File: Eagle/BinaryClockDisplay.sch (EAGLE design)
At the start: 44 parts

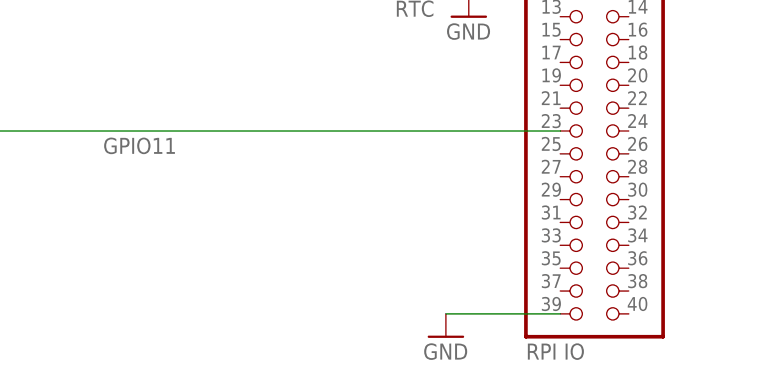
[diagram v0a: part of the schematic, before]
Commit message: Cleaning out some unused files
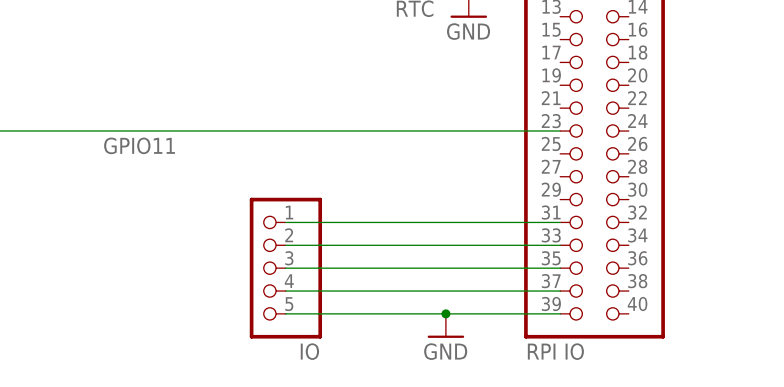
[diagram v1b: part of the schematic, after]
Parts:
- added JP4: IO, pinhead:PINHD-1X5
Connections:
- new net GPIO13: JP2.33, JP4.2
- new net GPIO19: JP2.35, JP4.3
- new net GPIO26: JP2.37, JP4.4
- new net GPIO6: JP2.31, JP4.1
- net GND: now also JP4.5
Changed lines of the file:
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@@
 <part name="JP1" library="pinhead" library_urn="urn:adsk.eagle:library:325" deviceset="PINHD-1X2" device="" package3d_urn="urn:adsk.eagle:package:22435/2"/>
 <part name="GND25" library="supply1" deviceset="GND" device=""/>
+<part name="JP4" library="pinhead" library_urn="urn:adsk.eagle:library:325" deviceset="PINHD-1X5" device="" package3d_urn="urn:adsk.eagle:package:22469/2" value="IO"/>
 </parts>
 <sheets>
@@
 <attribute name="VALUE" x="200.66" y="81.28" size="1.778" layer="96"/>
 </instance>
+<instance part="JP4" gate="A" x="177.8" y="2.54" smashed="yes" rot="MR0">
+<attribute name="VALUE" x="184.15" y="-7.62" size="1.778" layer="96" rot="MR0"/>
+</instance>
 </instances>
 <busses>
@@
 <pinref part="GND23" gate="1" pin="GND"/>
 <wire x1="210.82" y1="-2.54" x2="198.12" y2="-2.54" width="0.1524" layer="91"/>
+<pinref part="JP4" gate="A" pin="5"/>
+<wire x1="180.34" y1="-2.54" x2="198.12" y2="-2.54" width="0.1524" layer="91"/>
+<junction x="198.12" y="-2.54"/>
 </segment>
 <segment>
@@
 </segment>
 </net>
+<net name="GPIO26" class="0">
+<segment>
+<pinref part="JP4" gate="A" pin="4"/>
+<pinref part="JP2" gate="A" pin="37"/>
+<wire x1="180.34" y1="0" x2="210.82" y2="0" width="0.1524" layer="91"/>
+</segment>
+</net>
+<net name="GPIO19" class="0">
+<segment>
+<pinref part="JP4" gate="A" pin="3"/>
+<pinref part="JP2" gate="A" pin="35"/>
+<wire x1="180.34" y1="2.54" x2="210.82" y2="2.54" width="0.1524" layer="91"/>
+</segment>
+</net>
+<net name="GPIO13" class="0">
+<segment>
+<pinref part="JP4" gate="A" pin="2"/>
+<pinref part="JP2" gate="A" pin="33"/>
+<wire x1="180.34" y1="5.08" x2="210.82" y2="5.08" width="0.1524" layer="91"/>
+</segment>
+</net>
+<net name="GPIO6" class="0">
+<segment>
+<pinref part="JP4" gate="A" pin="1"/>
+<pinref part="JP2" gate="A" pin="31"/>
+<wire x1="180.34" y1="7.62" x2="210.82" y2="7.62" width="0.1524" layer="91"/>
+</segment>
+</net>

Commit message: HW version 2 allmost done...
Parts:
- added S2, S3: SWITCH, SparkFun-Electromechanical:SWITCH-MOMENTARY-2SMD-1101NE
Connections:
- new net GPIO10: JP2.19, S3.2
- new net GPIO9: JP2.21, S2.2
- net GND: now also S2.1, S3.1
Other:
- moved on the sheet: C4, D1, S1
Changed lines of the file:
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@@
 <part name="GND25" library="supply1" deviceset="GND" device=""/>
 <part name="JP4" library="pinhead" library_urn="urn:adsk.eagle:library:325" deviceset="PINHD-1X5" device="" package3d_urn="urn:adsk.eagle:package:22469/2" value="IO"/>
+<part name="S2" library="SparkFun-Electromechanical" deviceset="SWITCH-MOMENTARY-2" device="SMD-1101NE" value="SWITCH"/>
+<part name="GND26" library="supply1" deviceset="GND" device=""/>
+<part name="S3" library="SparkFun-Electromechanical" deviceset="SWITCH-MOMENTARY-2" device="SMD-1101NE" value="SWITCH"/>
+<part name="GND27" library="supply1" deviceset="GND" device=""/>
 </parts>
 <sheets>
@@
 </plain>
 <instances>
-<instance part="D1" gate="G$1" x="129.54" y="35.56" smashed="yes">
-<attribute name="NAME" x="116.84" y="43.942" size="1.778" layer="95"/>
-<attribute name="VALUE" x="116.84" y="27.94" size="1.778" layer="95"/>
+<instance part="D1" gate="G$1" x="129.54" y="40.64" smashed="yes">
+<attribute name="NAME" x="116.84" y="49.022" size="1.778" layer="95"/>
+<attribute name="VALUE" x="116.84" y="33.02" size="1.778" layer="95"/>
 </instance>
 <instance part="JP2" gate="A" x="213.36" y="22.86" smashed="yes">
@@
 <attribute name="VALUE" x="207.01" y="-7.62" size="1.778" layer="96"/>
 </instance>
-<instance part="C4" gate="G$1" x="104.14" y="35.56" smashed="yes">
-<attribute name="NAME" x="105.664" y="38.481" size="1.778" layer="95"/>
-<attribute name="VALUE" x="105.664" y="33.401" size="1.778" layer="96"/>
+<instance part="C4" gate="G$1" x="104.14" y="40.64" smashed="yes">
+<attribute name="NAME" x="105.664" y="43.561" size="1.778" layer="95"/>
+<attribute name="VALUE" x="105.664" y="38.481" size="1.778" layer="96"/>
 </instance>
 <instance part="JP3" gate="A" x="190.5" y="40.64" smashed="yes" rot="MR0">
@@
 <attribute name="VALUE" x="196.85" y="30.48" size="1.778" layer="96" rot="MR0"/>
 </instance>
-<instance part="GND10" gate="1" x="104.14" y="25.4" smashed="yes">
-<attribute name="VALUE" x="101.6" y="22.86" size="1.778" layer="96"/>
+<instance part="GND10" gate="1" x="104.14" y="30.48" smashed="yes">
+<attribute name="VALUE" x="101.6" y="27.94" size="1.778" layer="96"/>
 </instance>
 <instance part="D2" gate="G$1" x="129.54" y="71.12" smashed="yes">
@@
 <attribute name="VALUE" x="-238.76" y="43.18" size="1.778" layer="96"/>
 </instance>
-<instance part="S1" gate="G$1" x="139.7" y="17.78" smashed="yes">
-<attribute name="NAME" x="137.16" y="20.32" size="1.778" layer="95"/>
-</instance>
-<instance part="GND22" gate="1" x="129.54" y="12.7" smashed="yes">
-<attribute name="VALUE" x="127" y="10.16" size="1.778" layer="96"/>
+<instance part="S1" gate="G$1" x="170.18" y="17.78" smashed="yes">
+<attribute name="NAME" x="170.18" y="12.7" size="1.778" layer="95"/>
+</instance>
+<instance part="GND22" gate="1" x="160.02" y="12.7" smashed="yes">
+<attribute name="VALUE" x="157.48" y="10.16" size="1.778" layer="96"/>
 </instance>
 <instance part="GND23" gate="1" x="198.12" y="-5.08" smashed="yes">
@@
 <instance part="JP4" gate="A" x="177.8" y="2.54" smashed="yes" rot="MR0">
 <attribute name="VALUE" x="184.15" y="-7.62" size="1.778" layer="96" rot="MR0"/>
+</instance>
+<instance part="S2" gate="G$1" x="152.4" y="20.32" smashed="yes">
+<attribute name="NAME" x="149.86" y="15.24" size="1.778" layer="95"/>
+</instance>
+<instance part="GND26" gate="1" x="142.24" y="12.7" smashed="yes">
+<attribute name="VALUE" x="139.7" y="10.16" size="1.778" layer="96"/>
+</instance>
+<instance part="S3" gate="G$1" x="134.62" y="22.86" smashed="yes">
+<attribute name="NAME" x="132.08" y="17.78" size="1.778" layer="95"/>
+</instance>
+<instance part="GND27" gate="1" x="124.46" y="12.7" smashed="yes">
+<attribute name="VALUE" x="121.92" y="10.16" size="1.778" layer="96"/>
 </instance>
 </instances>
@@
 <pinref part="D1" gate="G$1" pin="VSS"/>
 <pinref part="C4" gate="G$1" pin="2"/>
-<wire x1="114.3" y1="33.02" x2="104.14" y2="33.02" width="0.1524" layer="91"/>
-<wire x1="104.14" y1="33.02" x2="104.14" y2="27.94" width="0.1524" layer="91"/>
-<junction x="104.14" y="33.02"/>
+<wire x1="114.3" y1="38.1" x2="104.14" y2="38.1" width="0.1524" layer="91"/>
+<wire x1="104.14" y1="38.1" x2="104.14" y2="33.02" width="0.1524" layer="91"/>
+<junction x="104.14" y="38.1"/>
 <pinref part="GND10" gate="1" pin="GND"/>
 </segment>
@@
 <pinref part="S1" gate="G$1" pin="1"/>
 <pinref part="GND22" gate="1" pin="GND"/>
-<wire x1="134.62" y1="17.78" x2="129.54" y2="17.78" width="0.1524" layer="91"/>
-<wire x1="129.54" y1="17.78" x2="129.54" y2="15.24" width="0.1524" layer="91"/>
+<wire x1="165.1" y1="17.78" x2="160.02" y2="17.78" width="0.1524" layer="91"/>
+<wire x1="160.02" y1="17.78" x2="160.02" y2="15.24" width="0.1524" layer="91"/>
 </segment>
 <segment>
@@
 <pinref part="GND25" gate="1" pin="GND"/>
 </segment>
+<segment>
+<pinref part="S2" gate="G$1" pin="1"/>
+<pinref part="GND26" gate="1" pin="GND"/>
+<wire x1="147.32" y1="20.32" x2="142.24" y2="20.32" width="0.1524" layer="91"/>
+<wire x1="142.24" y1="20.32" x2="142.24" y2="15.24" width="0.1524" layer="91"/>
+</segment>
+<segment>
+<pinref part="S3" gate="G$1" pin="1"/>
+<pinref part="GND27" gate="1" pin="GND"/>
+<wire x1="129.54" y1="22.86" x2="124.46" y2="22.86" width="0.1524" layer="91"/>
+<wire x1="124.46" y1="22.86" x2="124.46" y2="15.24" width="0.1524" layer="91"/>
+</segment>
 </net>
 <net name="N$2" class="0">
@@
 <segment>
 <pinref part="D1" gate="G$1" pin="DO"/>
-<wire x1="142.24" y1="33.02" x2="152.4" y2="33.02" width="0.1524" layer="91"/>
+<wire x1="142.24" y1="38.1" x2="152.4" y2="38.1" width="0.1524" layer="91"/>
 <pinref part="D2" gate="G$1" pin="DI"/>
-<wire x1="152.4" y1="33.02" x2="152.4" y2="76.2" width="0.1524" layer="91"/>
+<wire x1="152.4" y1="38.1" x2="152.4" y2="76.2" width="0.1524" layer="91"/>
 <wire x1="152.4" y1="76.2" x2="142.24" y2="76.2" width="0.1524" layer="91"/>
 </segment>
@@
 <segment>
 <pinref part="D1" gate="G$1" pin="DI"/>
-<wire x1="172.72" y1="40.64" x2="142.24" y2="40.64" width="0.1524" layer="91"/>
-<wire x1="233.68" y1="66.04" x2="172.72" y2="66.04" width="0.1524" layer="91"/>
-<wire x1="172.72" y1="66.04" x2="172.72" y2="40.64" width="0.1524" layer="91"/>
+<wire x1="175.26" y1="40.64" x2="142.24" y2="45.72" width="0.1524" layer="91"/>
+<wire x1="233.68" y1="66.04" x2="175.26" y2="66.04" width="0.1524" layer="91"/>
+<wire x1="175.26" y1="66.04" x2="175.26" y2="40.64" width="0.1524" layer="91"/>
 <label x="160.02" y="45.72" size="1.778" layer="95"/>
 <wire x1="233.68" y1="66.04" x2="233.68" y2="33.02" width="0.1524" layer="91"/>
@@
 <pinref part="S1" gate="G$1" pin="2"/>
 <pinref part="JP2" gate="A" pin="23"/>
-<wire x1="144.78" y1="17.78" x2="210.82" y2="17.78" width="0.1524" layer="91"/>
-<label x="160.02" y="15.24" size="1.778" layer="95"/>
+<wire x1="175.26" y1="17.78" x2="210.82" y2="17.78" width="0.1524" layer="91"/>
+<label x="180.34" y="15.24" size="1.778" layer="95"/>
 </segment>
 </net>
@@
 <pinref part="C4" gate="G$1" pin="1"/>
 <pinref part="D1" gate="G$1" pin="VDD"/>
-<wire x1="104.14" y1="40.64" x2="114.3" y2="40.64" width="0.1524" layer="91"/>
-<wire x1="104.14" y1="40.64" x2="104.14" y2="45.72" width="0.1524" layer="91"/>
-<junction x="104.14" y="40.64"/>
+<wire x1="104.14" y1="45.72" x2="114.3" y2="45.72" width="0.1524" layer="91"/>
+<wire x1="104.14" y1="45.72" x2="104.14" y2="50.8" width="0.1524" layer="91"/>
+<junction x="104.14" y="45.72"/>
 </segment>
 <segment>
@@
 </segment>
 </net>
+<net name="GPIO9" class="0">
+<segment>
+<pinref part="S2" gate="G$1" pin="2"/>
+<wire x1="157.48" y1="20.32" x2="210.82" y2="20.32" width="0.1524" layer="91"/>
+<pinref part="JP2" gate="A" pin="21"/>
+</segment>
+</net>
+<net name="GPIO10" class="0">
+<segment>
+<pinref part="S3" gate="G$1" pin="2"/>
+<pinref part="JP2" gate="A" pin="19"/>
+<wire x1="139.7" y1="22.86" x2="210.82" y2="22.86" width="0.1524" layer="91"/>
+</segment>
+</net>
